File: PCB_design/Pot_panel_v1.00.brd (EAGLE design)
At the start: 100 x 80 mm, 5 parts

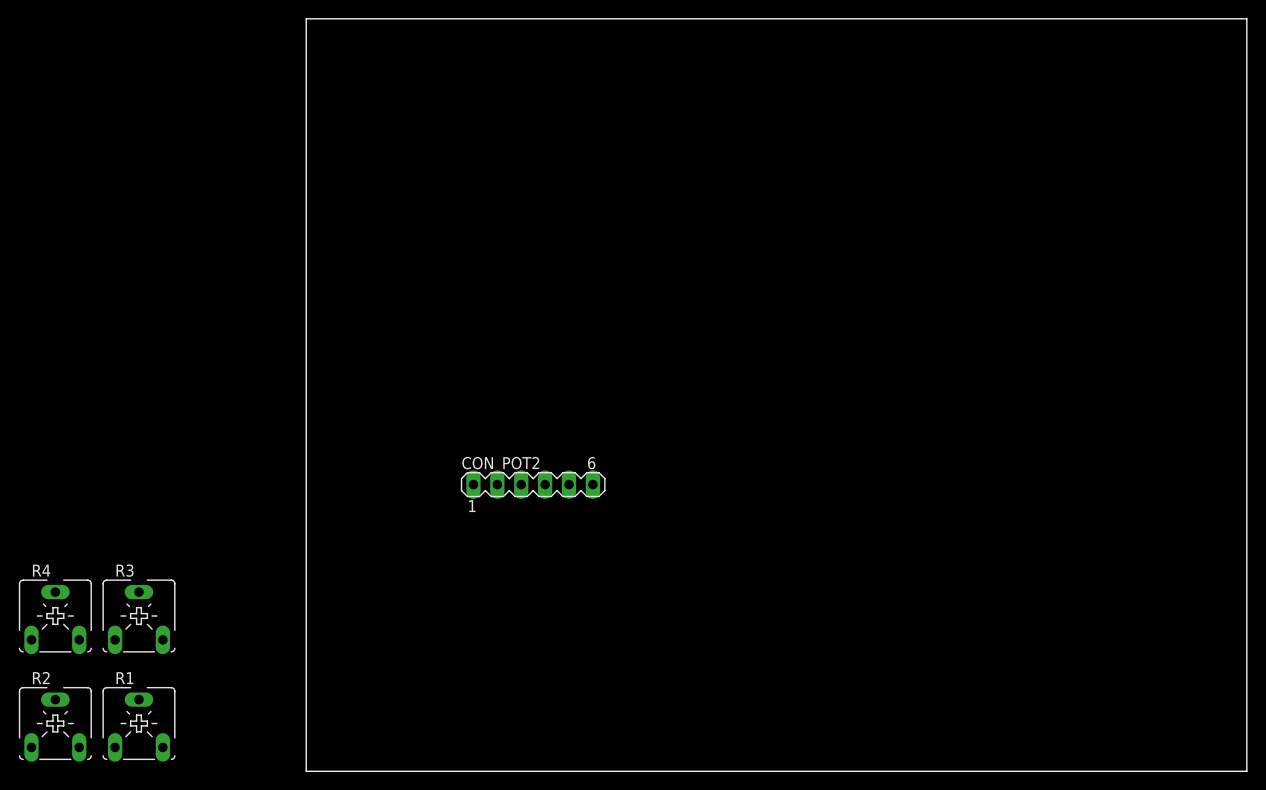
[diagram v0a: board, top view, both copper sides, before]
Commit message: Change arduino layout to fit to the buyable clone
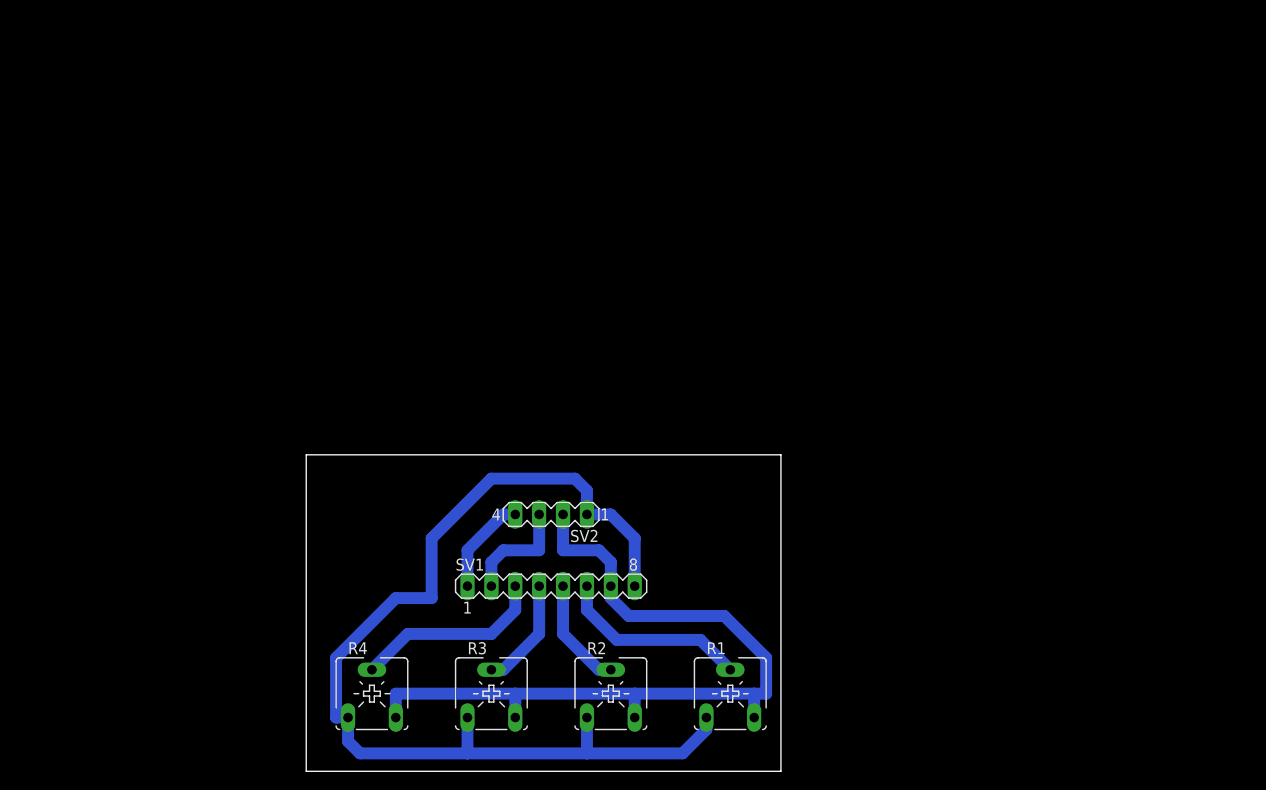
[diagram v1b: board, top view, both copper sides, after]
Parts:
- removed CON_POT2: (no value), con-lstb:MA06-1
- added SV1: (no value), con-lstb:MA08-1
- added SV2: (no value), con-lstb:MA04-1
- moved R1 62.9 mm to (45.1, 8.26)
- moved R2 59.1 mm to (32.4, 8.26)
- moved R3 38.4 mm to (19.7, 8.26)
- moved R4 34.7 mm to (6.99, 8.26)
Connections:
- new net N$1: SV1.1, SV2.4
- new net N$2: SV1.2, SV2.3
- net A0: now also SV1.6; no longer CON_POT2.4
- net A1: now also SV1.5; no longer CON_POT2.3
- net A2: now also SV1.4; no longer CON_POT2.2
- net A3: now also SV1.3; no longer CON_POT2.1
- net GND: now also SV1.8, SV2.1; no longer CON_POT2.6
- net VCC: now also SV1.7, SV2.2; no longer CON_POT2.5
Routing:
- net GND: track 0.00 -> 111.3 mm
- net VCC: track 0.00 -> 85.7 mm
- net A3: track 0.00 -> 20.4 mm
- net A0: track 0.00 -> 20.4 mm
- net N$2: track 0.00 -> 12.0 mm
- net A2: track 0.00 -> 11.7 mm
- net A1: track 0.00 -> 11.7 mm
- net N$1: track 0.00 -> 10.5 mm
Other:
- board size 100 x 80 mm -> 50.5 x 33.6 mm
